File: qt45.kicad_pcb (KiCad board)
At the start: 2 copper layers, 266.7 x 81 mm, 106 parts, among them SW1 SW_PUSH, U1 ATmega32U4-AU, Y1 16MHz

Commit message: Add branding and adjust silkscreen
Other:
- board text added: "qt45 by /u/bnhw github.com/qtkb/qt45-pcb"
- board text added: "u r a qt 2"

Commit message: Fix some issues
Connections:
- U1 pad 19: ROW2 -> Net-(U1-Pad19)
- U1 pad 21: Net-(U1-Pad21) -> ROW2
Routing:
- net GND: track 217.9 -> 213.7 mm
- net ROW1: track 286.4 -> 289.6 mm
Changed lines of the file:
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@@
     (thickness 1.6)
     (drawings 162)
-    (tracks 638)
+    (tracks 642)
     (zones 0)
     (modules 106)
@@
   (net 83 "Net-(USB1-Pad6)")
   (net 84 "Net-(U1-Pad20)")
-  (net 85 "Net-(U1-Pad21)")
+  (net 85 "Net-(U1-Pad19)")
   (net_class Default "This is the default net class."
     (clearance 0.2)
@@
     (add_net "Net-(U1-Pad11)")
     (add_net "Net-(U1-Pad12)")
+    (add_net "Net-(U1-Pad19)")
     (add_net "Net-(U1-Pad20)")
-    (add_net "Net-(U1-Pad21)")
     (add_net "Net-(U1-Pad42)")
     (add_net "Net-(U1-Pad8)")
@@
       (net 18 ROW3))
     (pad 19 smd rect (at 1.6 -5.7) (size 1.5 0.55) (layers B.Cu B.Paste B.Mask)
-      (net 13 ROW2))
+      (net 85 "Net-(U1-Pad19)"))
     (pad 20 smd rect (at 2.4 -5.7) (size 1.5 0.55) (layers B.Cu B.Paste B.Mask)
       (net 84 "Net-(U1-Pad20)"))
     (pad 21 smd rect (at 3.2 -5.7) (size 1.5 0.55) (layers B.Cu B.Paste B.Mask)
-      (net 85 "Net-(U1-Pad21)"))
+      (net 13 ROW2))
     (pad 22 smd rect (at 4 -5.7) (size 1.5 0.55) (layers B.Cu B.Paste B.Mask)
       (net 61 COL5))
@@
   (segment (start 94.19649 136.78999) (end 94.19649 133.64703) (width 0.381) (layer B.Cu) (net 1))
   (segment (start 95.0745 137.668) (end 94.19649 136.78999) (width 0.381) (layer B.Cu) (net 1))
-  (via (at 176.056901 129.066901) (size 0.8) (drill 0.4) (layers F.Cu B.Cu) (net 1))
-  (segment (start 176.056901 129.085099) (end 176.056901 129.066901) (width 0.381) (layer F.Cu) (net 1))
-  (segment (start 173.557 131.585) (end 176.056901 129.085099) (width 0.381) (layer F.Cu) (net 1))
-  (segment (start 173.557 132.516) (end 173.557 131.585) (width 0.381) (layer F.Cu) (net 1))
-  (segment (start 176.056901 129.066901) (end 150.042343 129.066901) (width 0.381) (layer B.Cu) (net 1))
   (segment (start 153.36351 102.92249) (end 146.705442 109.580558) (width 0.381) (layer B.Cu) (net 1))
   (segment (start 153.36351 84.298576) (end 153.36351 102.92249) (width 0.381) (layer B.Cu) (net 1))
@@
   (segment (start 137.191442 140.589) (end 143.755501 134.024941) (width 0.381) (layer B.Cu) (net 1))
   (segment (start 131.1125 140.589) (end 137.191442 140.589) (width 0.381) (layer B.Cu) (net 1))
+  (via (at 173.609 130.937) (size 0.8) (drill 0.4) (layers F.Cu B.Cu) (net 1))
+  (segment (start 173.557 132.516) (end 173.557 130.989) (width 0.381) (layer F.Cu) (net 1))
+  (segment (start 173.557 130.989) (end 173.609 130.937) (width 0.381) (layer F.Cu) (net 1))
+  (segment (start 172.304586 129.066901) (end 171.542099 129.066901) (width 0.381) (layer B.Cu) (net 1))
+  (segment (start 173.609 130.371315) (end 172.304586 129.066901) (width 0.381) (layer B.Cu) (net 1))
+  (segment (start 173.609 130.937) (end 173.609 130.371315) (width 0.381) (layer B.Cu) (net 1))
+  (segment (start 171.542099 129.066901) (end 150.042343 129.066901) (width 0.381) (layer B.Cu) (net 1))
   (segment (start 107.679903 133.582031) (end 107.679903 133.482031) (width 0.254) (layer B.Cu) (net 2))
   (segment (start 108.971872 134.874) (end 107.679903 133.582031) (width 0.254) (layer B.Cu) (net 2))
@@
   (segment (start 130.717 101.854) (end 115.3455 101.854) (width 0.254) (layer B.Cu) (net 8))
   (segment (start 131.70225 100.86875) (end 130.717 101.854) (width 0.254) (layer B.Cu) (net 8))
-  (segment (start 132.55625 100.86875) (end 131.70225 100.86875) (width 0.254) (layer B.Cu) (net 8))
+  (segment (start 131.70225 100.86875) (end 132.55625 100.86875) (width 0.254) (layer B.Cu) (net 8))
+  (segment (start 133.41025 100.86875) (end 135.763 100.86875) (width 0.254) (layer B.Cu) (net 8))
+  (segment (start 132.55625 100.86875) (end 133.41025 100.86875) (width 0.254) (layer B.Cu) (net 8))
   (segment (start 34.925 97.155) (end 34.925 97.56875) (width 0.254) (layer B.Cu) (net 9))
   (segment (start 29.5275 91.7575) (end 34.925 97.155) (width 0.254) (layer B.Cu) (net 9))
@@
   (segment (start 50.95875 91.7575) (end 56.35625 97.155) (width 0.254) (layer B.Cu) (net 12))
   (segment (start 101.619148 119.91875) (end 101.24975 119.91875) (width 0.254) (layer B.Cu) (net 13))
-  (segment (start 113.374398 131.674) (end 101.619148 119.91875) (width 0.254) (layer B.Cu) (net 13))
-  (segment (start 114.188 131.674) (end 113.374398 131.674) (width 0.254) (layer B.Cu) (net 13))
   (segment (start 126.20625 119.91875) (end 101.24975 119.91875) (width 0.254) (layer B.Cu) (net 13))
   (segment (start 101.24975 119.91875) (end 39.6875 119.91875) (width 0.254) (layer B.Cu) (net 13))
@@
   (segment (start 164.30625 119.91875) (end 199.23125 119.91875) (width 0.254) (layer B.Cu) (net 13))
   (segment (start 161.13125 119.91875) (end 164.30625 119.91875) (width 0.254) (layer B.Cu) (net 13))
+  (segment (start 113.374398 131.674) (end 101.619148 119.91875) (width 0.254) (layer B.Cu) (net 13))
+  (segment (start 113.374398 131.674) (end 114.188 131.674) (width 0.254) (layer B.Cu) (net 13))
   (segment (start 70.64375 78.105) (end 70.64375 78.51875) (width 0.254) (layer B.Cu) (net 14))
   (segment (start 65.24625 72.7075) (end 70.64375 78.105) (width 0.254) (layer B.Cu) (net 14))

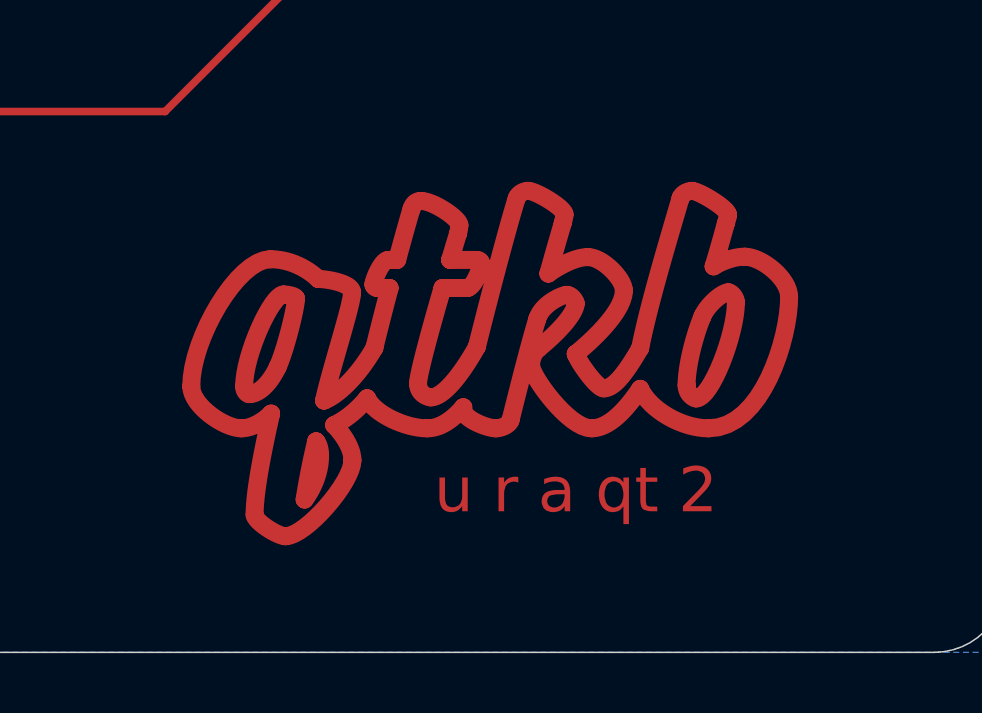
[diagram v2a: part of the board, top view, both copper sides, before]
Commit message: Increase size of copper in logo and add version number
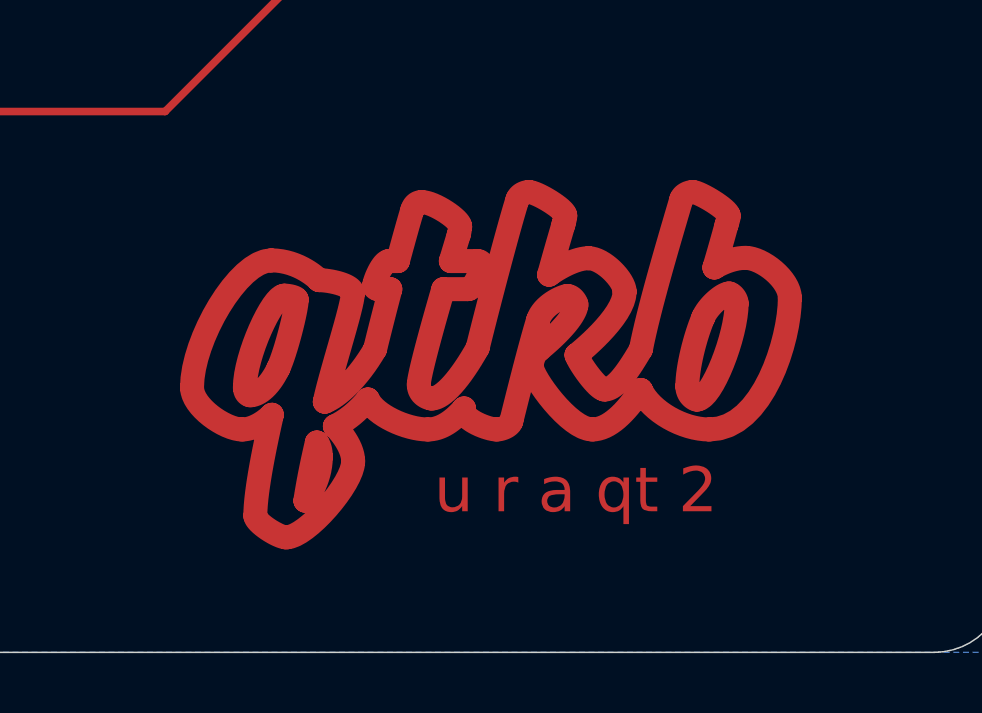
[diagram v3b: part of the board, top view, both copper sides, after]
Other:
- board text added: "qt45 v1 by /u/bnhw github.com/qtkb/qt45-pcb"
- board text removed: "qt45 by /u/bnhw github.com/qtkb/qt45-pcb"

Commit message: Add front ground plane
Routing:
- net GND: track 213.7 -> 229.1 mm, vias 1 -> 45
- net COL10: track 155.6 -> 154.8 mm
- net COL7: vias 3 -> 2
- added copper zone on F.Cu, net GND
